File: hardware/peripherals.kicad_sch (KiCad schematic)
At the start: 40 parts, among them J2 Conn_01x02, J3 Conn_01x02, J4 Conn_01x02, J5 Conn_01x02, U2 BNO055, Y1 32.768k

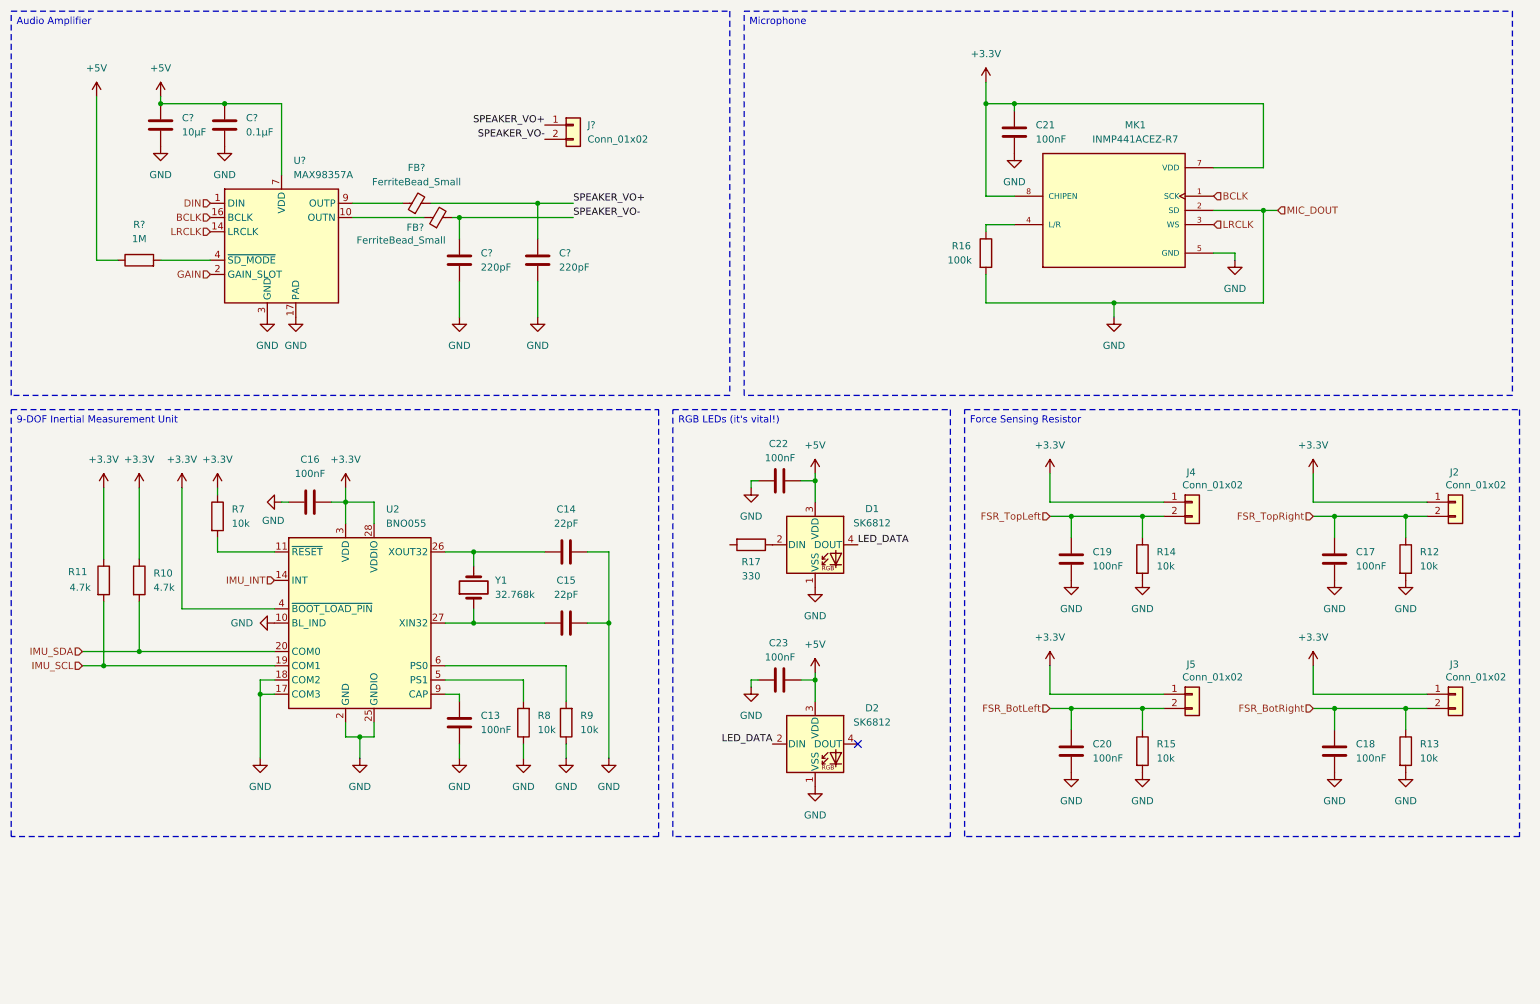
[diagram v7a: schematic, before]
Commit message: Adding BMS
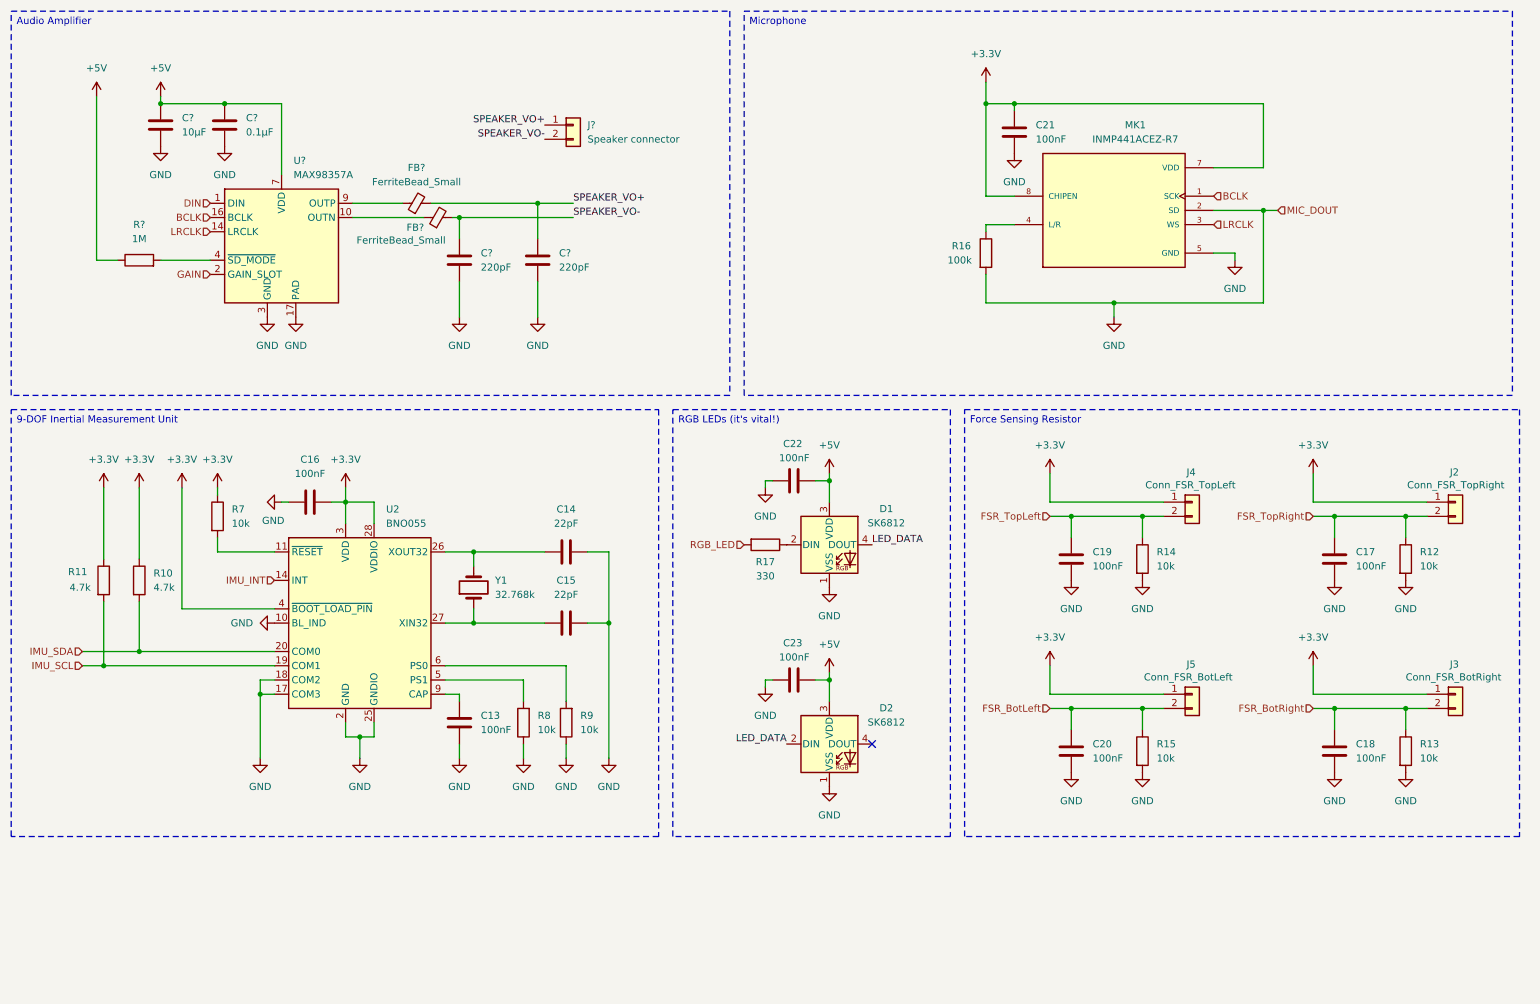
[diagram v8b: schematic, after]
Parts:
- J2: value Conn_01x02 -> Conn_FSR_TopRight
- J3: value Conn_01x02 -> Conn_FSR_BotRight
- J4: value Conn_01x02 -> Conn_FSR_TopLeft
- J5: value Conn_01x02 -> Conn_FSR_BotLeft
- J?: value Conn_01x02 -> Speaker connector
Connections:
- net RGB_LED: now reaches R17.2
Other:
- moved on the sheet: C22, C23, D1, D2, R17
